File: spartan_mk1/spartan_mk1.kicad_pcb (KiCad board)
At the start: 4 copper layers, 43.2 x 40.6 mm, 92 parts, among them J1 USB_B_Micro, J10 Conn_01x02_Female, J11 Conn_01x02_Female, J12 Conn_01x02_Female, J13 Conn_02x05_Odd_Even, J14 Conn_01x02_Female, J15 Conn_01x08_Female, J16 Conn_01x02_Female, J17 Conn_01x02_Female, J18 Conn_01x08_Female, J2 Conn_01x02_Female, J3 Conn_01x02_Female, J4 Conn_01x02_Female, J5 Conn_01x02_Female, J6 Conn_01x02_Female, J7 Conn_01x04_Female, J8 Conn_01x03_Female, J9 Conn_01x03_Female, Q1 2N7002, Q2 2N7002, Q3 AO3401A, U1 MPU-6050, U2 AT24C256C-SSHL-T, U3 USBLC6-2SC6, U4 STM32F405RGTx, U5 NCP1117-3.3_TO252, U6 TPS5430DDA, Y1 X322516MLB4SI

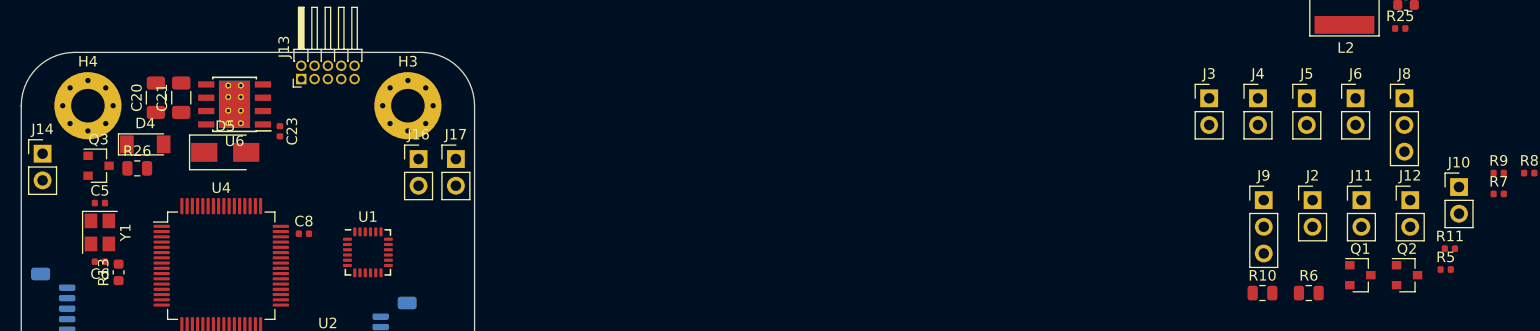
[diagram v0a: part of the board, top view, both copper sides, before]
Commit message: Changed offboard connections to SMD pads for space
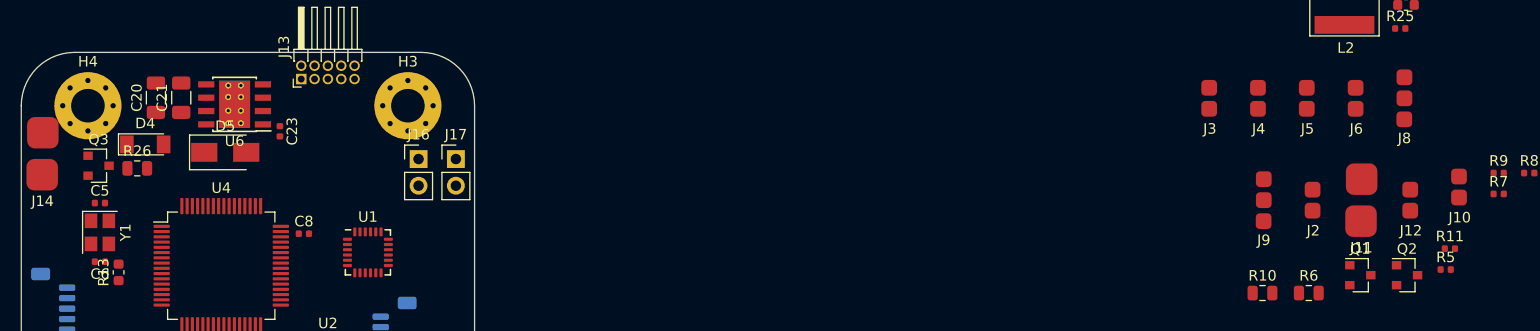
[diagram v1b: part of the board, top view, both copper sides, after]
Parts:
- J10, J12, J2, J3, J4, J5, J6: footprint Connector_PinHeader_2.54mm:PinHeader_1x02_P2.54mm_Vertical -> Connector_SMD:01x02_1.5mm
- J11, J14: footprint Connector_PinHeader_2.54mm:PinHeader_1x02_P2.54mm_Vertical -> Connector_SMD:01x02_3mm
- J8, J9: footprint Connector_PinHeader_2.54mm:PinHeader_1x03_P2.54mm_Vertical -> Connector_SMD:01x03_1.5mm
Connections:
- C8 pad 2: GND -> Net-(C8-Pad2)

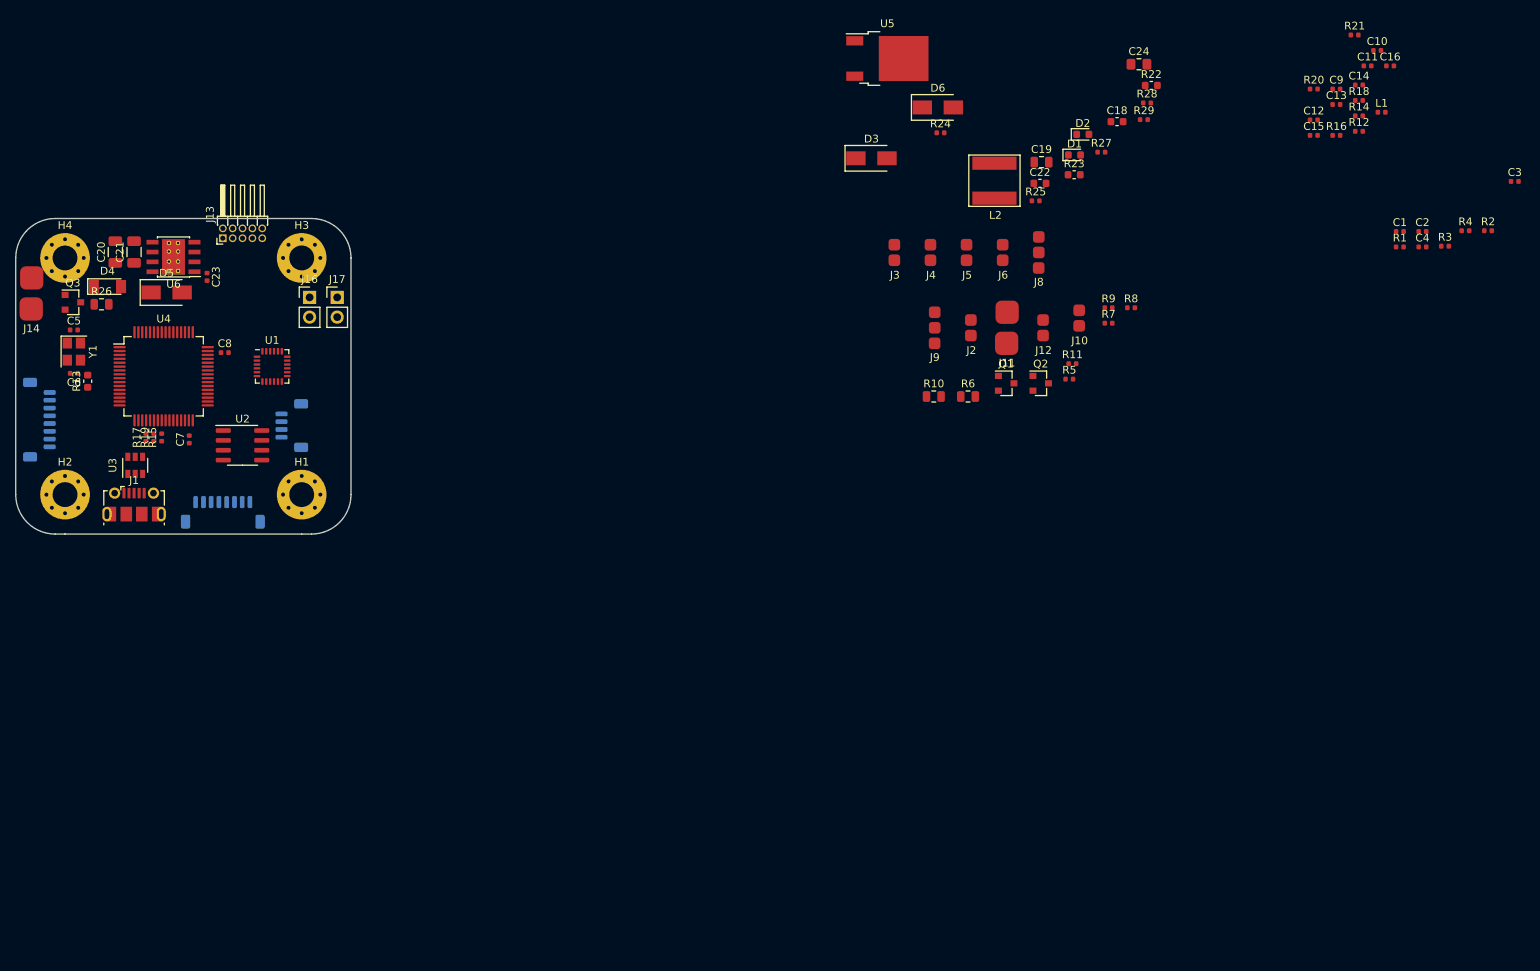
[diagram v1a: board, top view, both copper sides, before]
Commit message: Almost complete PCB layout (no routing)
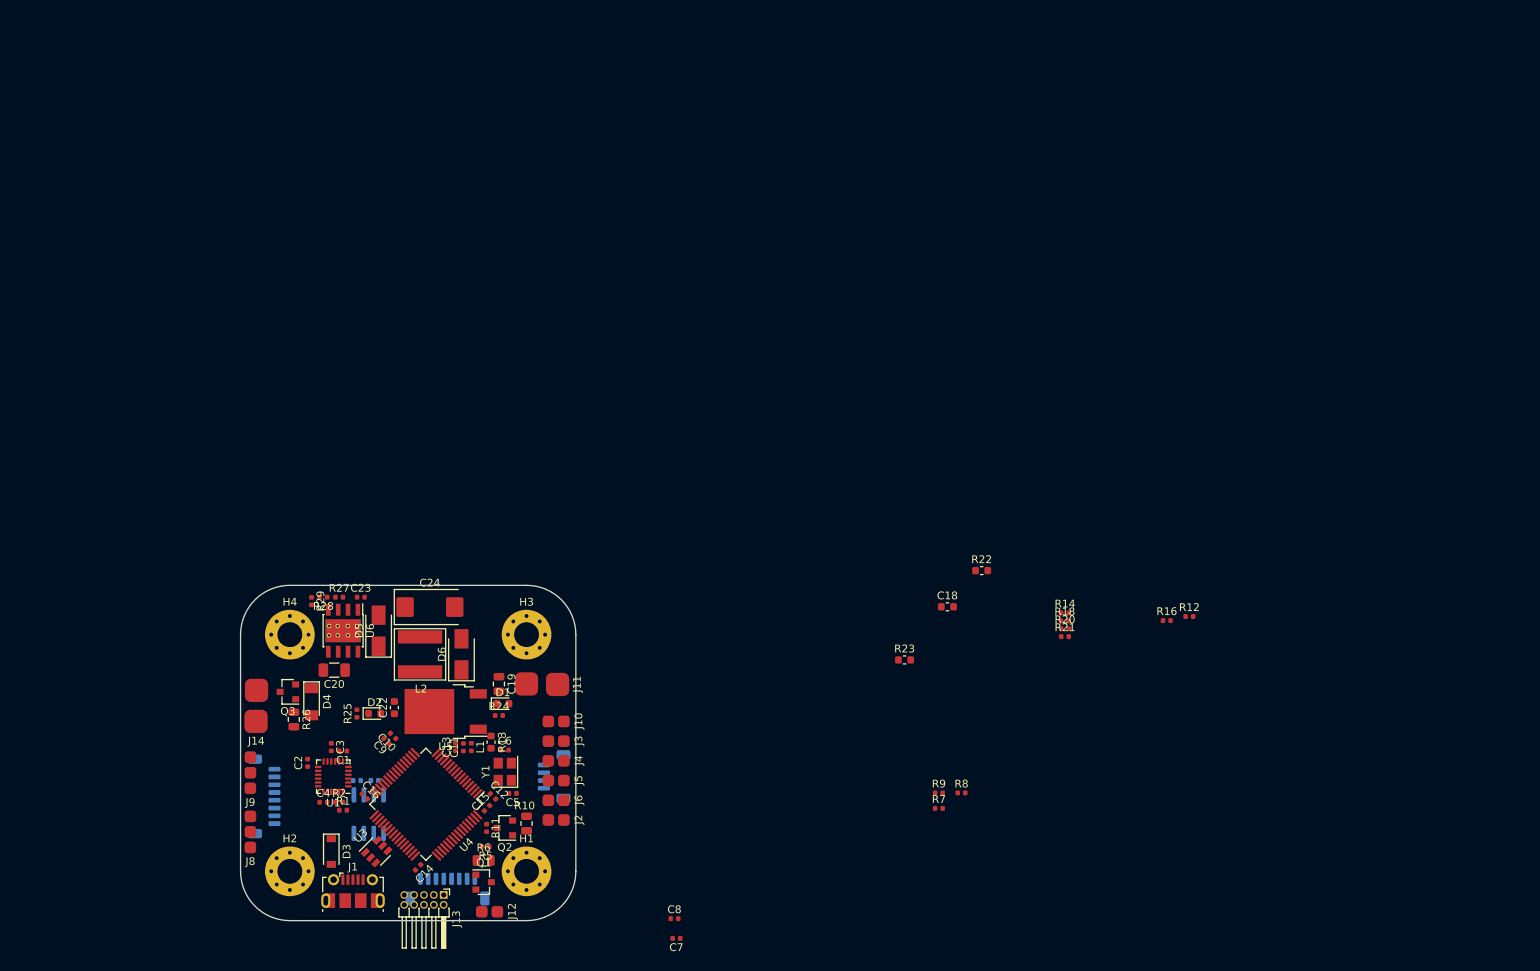
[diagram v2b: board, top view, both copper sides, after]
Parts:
- removed C21: 10uf, Capacitor_SMD:C_1206_3216Metric
- removed J16, J17: Conn_01x02_Female, Connector_PinHeader_2.54mm:PinHeader_1x02_P2.54mm_Vertical
- removed R15, R17, R19: 0R, Resistor_SMD:R_0402_1005Metric
- C24: footprint Capacitor_SMD:C_0805_2012Metric_Pad1.15x1.40mm_HandSolder -> Capacitor_Tantalum_SMD:CP_EIA-7343-43_Kemet-X_Pad2.25x2.55mm_HandSolder
- D3: footprint Diode_SMD:D_SMA -> Diode_SMD:D_SOD-123
- R3, R4, U2: moved to B.Cu
- moved C3 168.9 mm to (124.5, 92.2), turned to 270 degrees
- moved R2 165.3 mm to (125.5, 99.3)
- moved C16 162.1 mm to (128.8, 98.6), turned to 315 degrees
- moved C2 159.0 mm to (121.4, 94.2), turned to 90 degrees
- moved C4 158.6 mm to (123.4, 99.3)
- moved C14 157.6 mm to (135.6, 107.7), turned to 225 degrees
- moved R4 157.3 mm to (130.0, 96.5)
- moved R3 156.1 mm to (127.8, 96.5), turned to 180 degrees
- moved C10 154.4 mm to (132.4, 90.8), turned to 135 degrees
- moved R1 154.2 mm to (126.0, 100.3)
- moved C1 151.6 mm to (126.0, 92.7), turned to 180 degrees
- moved C9 148.4 mm to (131.6, 91.4), turned to 135 degrees
- moved C11 145.8 mm to (141.5, 92.2), turned to 90 degrees
- moved L1 142.9 mm to (142.5, 92.2), turned to 270 degrees
- moved C13 140.4 mm to (140.5, 92.2), turned to 90 degrees
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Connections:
- R16 pad 2: Net-(R16-Pad2) -> /SPI_ESC_MISO
- U4 pad 21: Net-(R17-Pad1) -> /SPI_ESC_SCK
- U4 pad 22: Net-(R16-Pad2) -> /SPI_ESC_MISO
- U4 pad 23: Net-(R15-Pad1) -> /SPI_ESC_MOSI
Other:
- board size 43.2 x 40.6 mm -> 43.2 x 43.2 mm
